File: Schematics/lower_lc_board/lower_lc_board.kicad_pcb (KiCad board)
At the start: 4 copper layers, 69.5 x 60 mm, 178 parts, among them J1 Stack Male Edge Connector, J10 SOL_CONN, J11 Screw_Terminal_01x02, J2 SWD_CONN, J3 USB_C_CONN, J4 HALL-1, J5 HALL-2, J6 PT1, J7 Screw_Terminal_01x02, J8 PT1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

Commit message: start lower refactor
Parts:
- removed J1: Stack Male Edge Connector, Connector_PCBEdge:BUS_PCIexpress_x1
- added REF**: TerminalBlock_TE_282834-2_1x02_P2.54mm_Horizontal, TerminalBlock_TE-Connectivity:TerminalBlock_TE_282834-2_1x02_P2.54mm_Horizontal, F.Cu at (129.5, 102.1)
- added REF**: TerminalBlock_TE_282834-2_1x02_P2.54mm_Horizontal, TerminalBlock_TE-Connectivity:TerminalBlock_TE_282834-2_1x02_P2.54mm_Horizontal, F.Cu at (136.9, 102.1)
- moved BZ1 30.0 mm to (202.0, 46.7)
- moved D8 30.0 mm to (202.2, 49.6)
- moved Q4 30.0 mm to (198.4, 48.8)
- moved R47 30.0 mm to (202.0, 51.4)
- moved C24 30.0 mm to (198.9, 51.4)
- moved R21 30.0 mm to (195.0, 46.7)
- moved R46 30.0 mm to (195.0, 48.3)
- moved C8 23.9 mm to (140.5, 117.8)
- moved R17 22.0 mm to (120.9, 114.0)
- moved C23 22.0 mm to (117.6, 116.0)
- moved J5 22.0 mm to (124.1, 114.0)
- moved R18 22.0 mm to (122.4, 113.9)
- moved C33 22.0 mm to (129.9, 116.9)
- moved J4 22.0 mm to (113.2, 114.0)
- moved C35 14.1 mm to (135.1, 117.1)
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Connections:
- J4 pad 1: GND -> +3V3
- J4 pad 4: +3V3 -> GND
- J5 pad 1: GND -> +3V3
- J5 pad 4: +3V3 -> GND
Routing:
- net +3V3: track 435.2 -> 356.2 mm, vias 20 -> 16
- net GND: track 236.0 -> 194.1 mm, vias 204 -> 194
- net HALL_SDA: track 57.6 -> 33.5 mm, vias 2 -> 1
- net /Sensing Circuitry/VPT: track 41.2 -> 19.7 mm
- net BUZZ_IN: track 18.0 -> 0.00 mm
- net Net-(BZ1--): track 16.5 -> 0.00 mm, vias 2 -> 0
- net +24V: track 133.7 -> 117.3 mm, vias 5 -> 3
- net HALL_SCL: track 50.1 -> 38.3 mm, vias 2 -> 1
- net VPT-SW: track 36.4 -> 24.9 mm, vias 2 -> 1
- net Net-(U11-G): track 7.76 -> 0.00 mm
- net +5V: track 67.7 -> 61.3 mm
- net +24V_BP: track 41.9 -> 36.0 mm
- net /Power Circuitry/3V3_BP: track 19.9 -> 14.8 mm
- net Net-(Q4-G): track 4.18 -> 0.00 mm
- net Net-(Q3-G): track 3.78 -> 0.00 mm
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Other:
- outline, holes or cut-outs redrawn

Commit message: start lower refactor
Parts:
- removed C12: 10uF, Capacitor_SMD:CP_Elec_4x5.4
- removed J11, J7: Screw_Terminal_01x02, TerminalBlock_TE-Connectivity:TerminalBlock_TE_282834-2_1x02_P2.54mm_Horizontal
- removed J6, J8: PT1, ul_B02B-PASK-1:CONN_B02B-PASK-1_JST
- removed the REF** at (129.5, 102.1)
- removed the REF** at (136.9, 102.1)
- added C1: 10uF, Capacitor_SMD:CP_Elec_4x5.4, F.Cu at (157.1, 62.5)
- added J1: Conn_01x06, CONN_SD-4:CONN_SD-43045-001_06_MOL, F.Cu at (163.7, 56.9)
- added REF**: MOLEX_1053091102, NANO-V-CONN:MOLEX_1053091102, F.Cu at (158.7, 124.2)
- added REF**: MOLEX_1053091102, NANO-V-CONN:MOLEX_1053091102, F.Cu at (153.9, 138.2)
- added REF**: CONN_SD-105309-100_04_MOL, NANO-V-4-CONN:CONN_SD-105309-100_04_MOL, F.Cu at (123.1, 102.8)
- added REF**: CONN_SD-105309-100_04_MOL, NANO-V-4-CONN:CONN_SD-105309-100_04_MOL, F.Cu at (130.2, 102.8)
- added REF**: MOLEX_1053091102, NANO-V-CONN:MOLEX_1053091102, F.Cu at (153.9, 146.0)
- added REF**: MOLEX_1053091102, NANO-V-CONN:MOLEX_1053091102, F.Cu at (165.8, 122.3)
- moved TH1 64.3 mm to (85.1, 81.0)
- moved U2 60.7 mm to (217.0, 91.6)
- moved C32 60.5 mm to (82.8, 91.8)
- moved C31 60.5 mm to (85.9, 91.8)
- moved R26 60.5 mm to (87.4, 91.8)
- moved R57 60.5 mm to (92.0, 91.8)
- moved C54 60.5 mm to (93.5, 91.8)
- moved C55 60.5 mm to (90.5, 91.8)
- moved R24 60.5 mm to (84.4, 91.8)
- moved R28 60.5 mm to (81.3, 91.8)
- moved R59 60.5 mm to (89.0, 91.8)
- moved R1 42.9 mm to (198.1, 68.2)
- moved D1 39.7 mm to (195.6, 76.2)
- moved C7 30.9 mm to (198.3, 58.8)
- moved TP1 26.6 mm to (194.4, 69.2)
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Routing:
- net +3V3: track 356.2 -> 202.8 mm, vias 16 -> 10
- net GND: track 194.1 -> 134.7 mm, vias 194 -> 156
- net +5V: track 61.3 -> 20.6 mm, vias 5 -> 1
- net Net-(D9B-K1A2): track 49.3 -> 25.0 mm, vias 3 -> 2
- net Net-(D9A-K3A4): track 53.7 -> 30.4 mm, vias 6 -> 5
- net CAN_P: track 20.6 -> 41.8 mm, vias 0 -> 1
- net CAN_N: track 21.3 -> 41.7 mm, vias 0 -> 1
- net Net-(D18B-K1A2): track 40.0 -> 21.1 mm, vias 3 -> 2
- net /Sensing Circuitry/VPT: track 19.7 -> 1.06 mm
- net +24V_BP: track 36.0 -> 20.1 mm
- net Net-(D18A-K3A4): track 37.1 -> 22.9 mm, vias 3 -> 2
- net HALL_SCL: track 38.3 -> 25.6 mm
- net /Sensing Circuitry/TC_P_1: track 11.7 -> 0.00 mm
- net /Sensing Circuitry/TC_N_2: track 10.9 -> 0.09 mm
- net HALL_SDA: track 33.5 -> 25.2 mm
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- removed copper zone on F.Cu, net /Power Circuitry/3V3_USB
- removed copper zone on B.Cu, net GND
- removed copper zone on In1.Cu, net GND
- removed copper zone on In2.Cu, net GND
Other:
- board text added: "2.6mm height between board and nano connector thing"
- board text removed: "+ SD SC -"
- board text removed: "3V3"
- board text removed: "HALL-1"
- board text removed: "HALL-2"
- board text removed: "LDO"
- board text removed: "PMUX"
- board text removed: "VBP"
- board text removed: "VFLTR"
- board text removed: "VOUT"
- board text removed: "VSWD"
- board text removed: "VUSB"

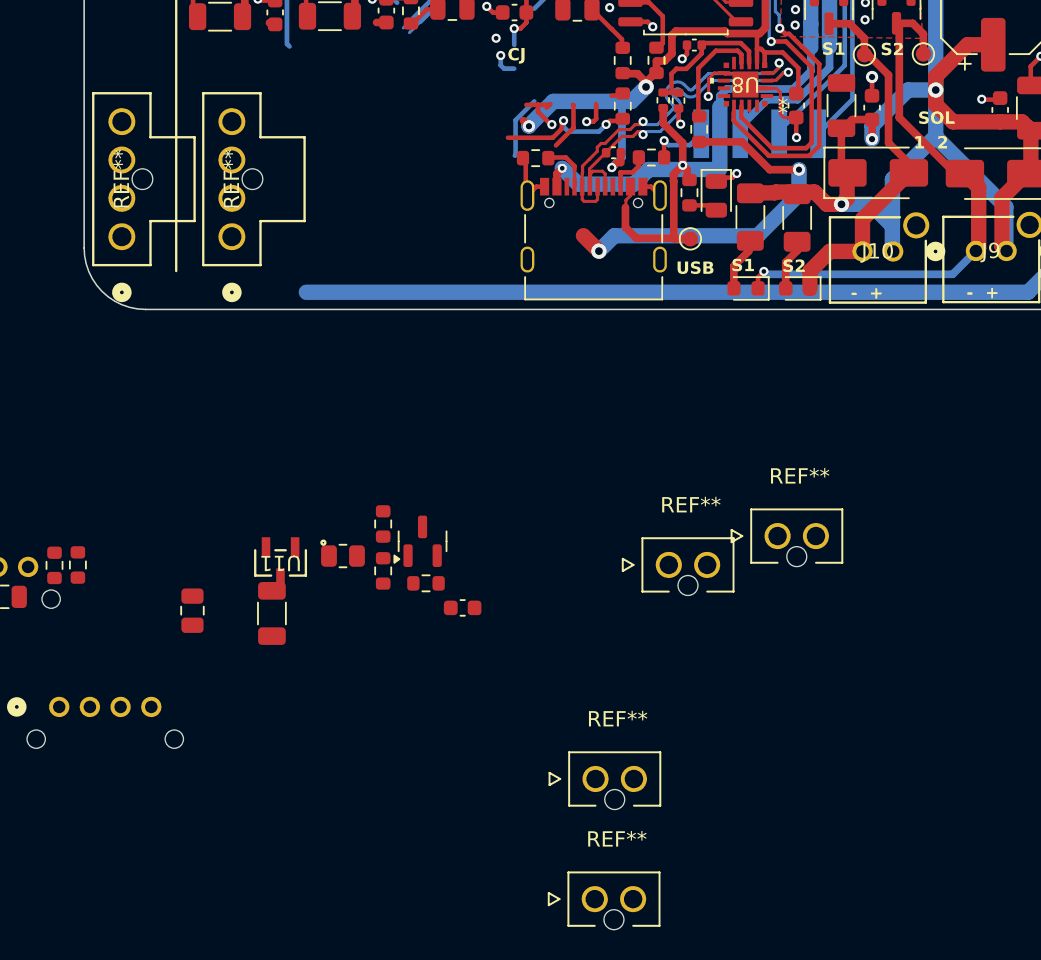
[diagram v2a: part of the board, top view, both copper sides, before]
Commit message: organize working copy of lower valve board for merge to main
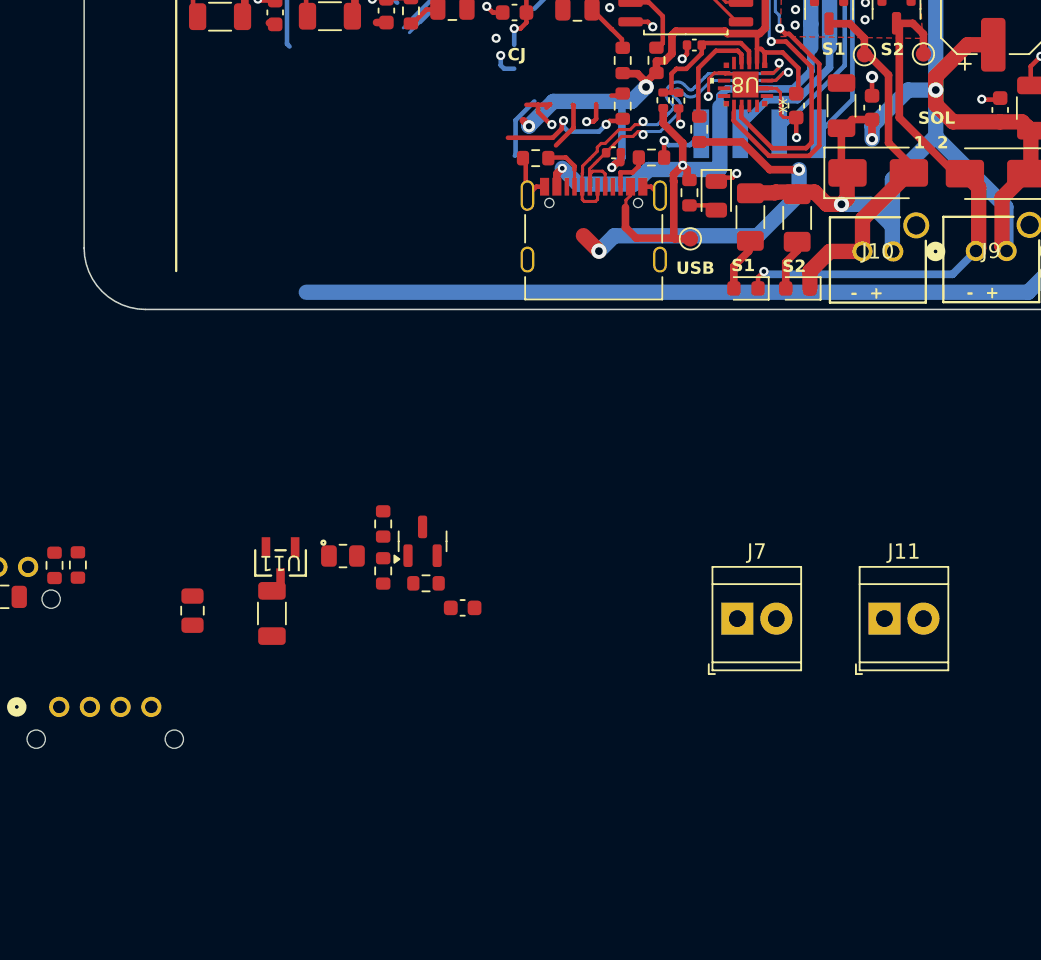
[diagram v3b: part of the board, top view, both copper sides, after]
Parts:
- removed REF** (x4): MOLEX_1053091102, NANO-V-CONN:MOLEX_1053091102
- removed REF** (x2): CONN_SD-105309-100_04_MOL, NANO-V-4-CONN:CONN_SD-105309-100_04_MOL
- added J11: Screw_Terminal_01x02, TerminalBlock_TE-Connectivity:TerminalBlock_TE_282834-2_1x02_P2.54mm_Horizontal, F.Cu at (172.8, 127.7)
- added J7: Screw_Terminal_01x02, TerminalBlock_TE-Connectivity:TerminalBlock_TE_282834-2_1x02_P2.54mm_Horizontal, F.Cu at (163.2, 127.7)

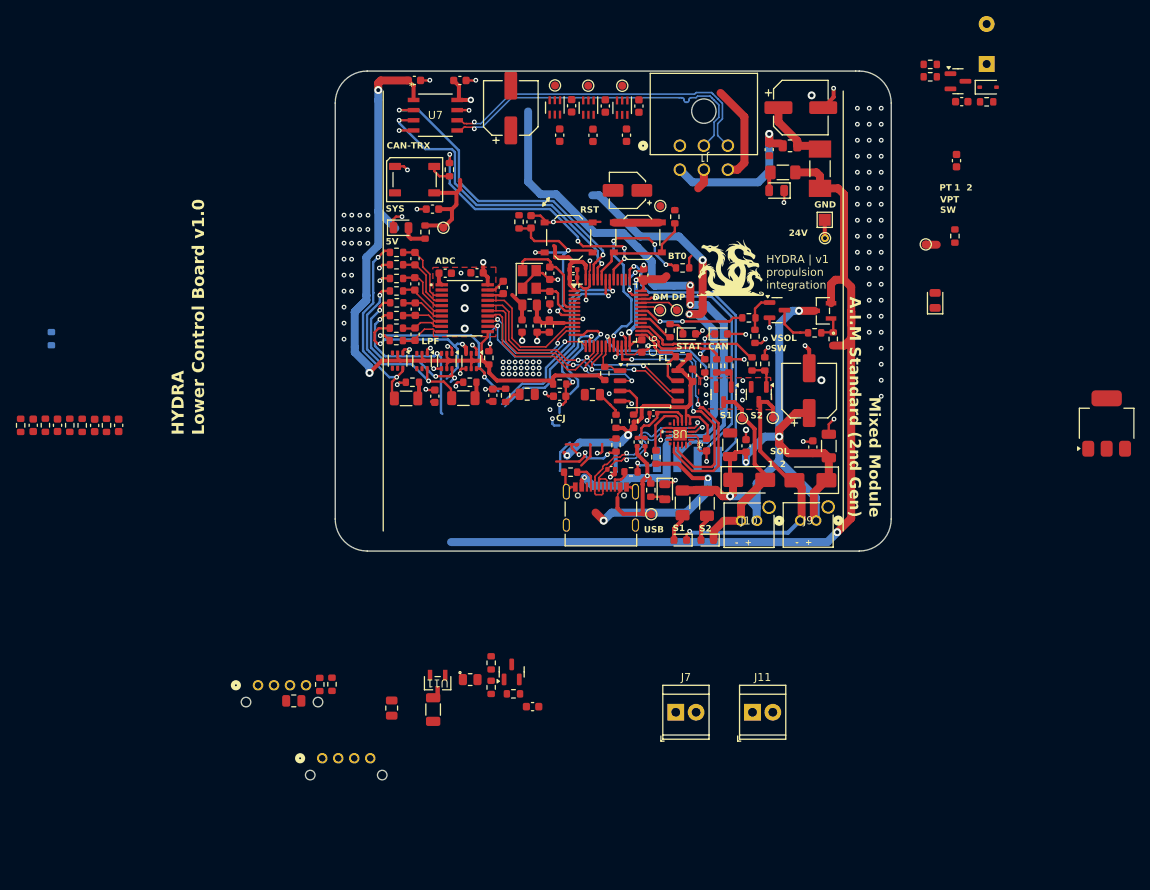
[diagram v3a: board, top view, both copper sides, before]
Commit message: lower refactor for review
 - curr using horziontal screw for TC
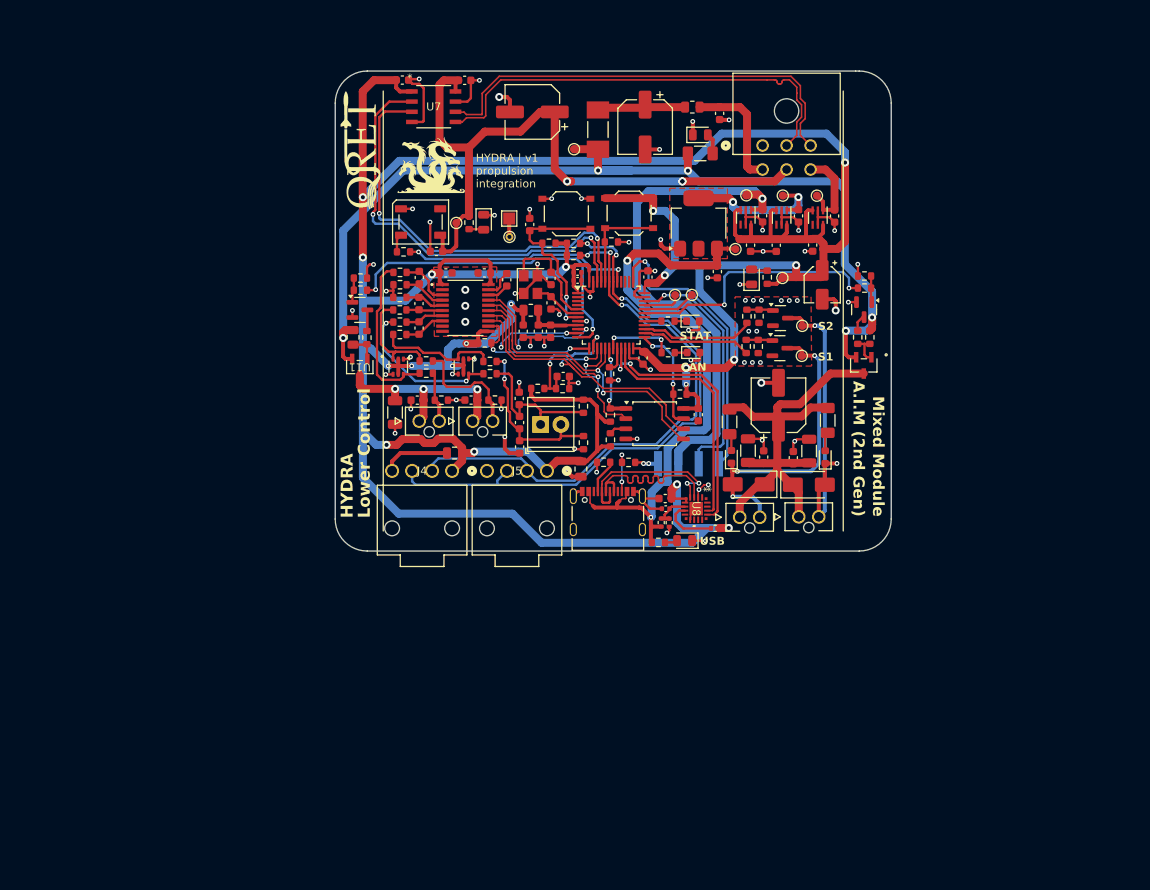
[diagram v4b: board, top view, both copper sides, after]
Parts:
- removed BZ1: Buzzer, Buzzer_Beeper:Buzzer_TDK_PS1240P02BT_D12.2mm_H6.5mm
- removed C24: 0.1uF, Capacitor_SMD:C_0603_1608Metric
- removed C25: 10nF, Capacitor_SMD:C_0603_1608Metric
- removed C53: 0.1uF, Capacitor_SMD:C_0805_2012Metric
- removed C54, C55: 1nF, Capacitor_SMD:C_0603_1608Metric
- removed the C8 at (145.3, 127.0)
- removed D14, D9: BAV199DW, Package_TO_SOT_SMD:SOT-363_SC-70-6
- removed D8: 1N4148WS-7-F, Diode_SMD:D_SOD-323
- removed J11: Screw_Terminal_01x02, TerminalBlock_TE-Connectivity:TerminalBlock_TE_282834-2_1x02_P2.54mm_Horizontal
- removed Q4: 2N7002, Package_TO_SOT_SMD:SOT-23
- removed R21: 10k, Resistor_SMD:R_0603_1608Metric
- removed R45: 1.5k, Capacitor_SMD:C_0402_1005Metric
- removed R46: 220, Resistor_SMD:R_0603_1608Metric
- removed R47, R55, R57: 1k, Resistor_SMD:R_0603_1608Metric
- removed R54, R59: 1M, Resistor_SMD:R_0603_1608Metric
- removed R56, R58: 200, Resistor_SMD:R_0603_1608Metric
- added J6: PT1, NANO-V-2-CONN:MOLEX_1053091102, F.Cu at (131.1, 91.3)
- added J8: PT1, NANO-V-2-CONN:MOLEX_1053091102, F.Cu at (137.8, 91.3)
- C30: footprint Capacitor_SMD:C_0805_2012Metric -> Capacitor_SMD:C_0603_1608Metric
- J10, J9: footprint ul_B02B-PASK-1:CONN_B02B-PASK-1_JST -> NANO-V-2-CONN:MOLEX_1053091102
- J4, J5: footprint S04B_PASK_2-P:CONN4_S04B-PASK_JST -> NANO-H-4-CONN:CONN_SD-105313-100_04_MOL; moved to F.Cu
- R13: footprint Resistor_SMD:R_0603_1608Metric -> Resistor_SMD:R_0402_1005Metric
- R32, R35: value 60 -> 62
- R33, R37: footprint Resistor_SMD:R_1206_3216Metric -> Resistor_SMD:R_0603_1608Metric
- TH1: moved to F.Cu
- moved R26 64.2 mm to (151.6, 89.5), turned to -90 degrees
- moved TH1 64.2 mm to (149.0, 87.2), turned to 0 degrees
- moved R18 62.8 mm to (150.4, 69.1), turned to 0 degrees
- moved R17 62.3 mm to (150.4, 70.6), turned to 180 degrees
- moved C32 60.9 mm to (143.7, 94.5)
- moved R28 59.2 mm to (139.9, 83.9), turned to 0 degrees
- moved C31 57.8 mm to (143.6, 88.5), turned to -90 degrees
- moved U2 56.8 mm to (166.0, 66.6)
- moved R24 56.0 mm to (139.9, 85.4), turned to 0 degrees
- moved R44 54.0 mm to (123.8, 74.9)
- moved R43 53.7 mm to (123.8, 73.4), turned to 180 degrees
- moved Q3 49.1 mm to (123.7, 77.4), turned to 0 degrees
- moved J5 45.6 mm to (147.1, 97.5)
- moved TP1 45.5 mm to (150.5, 57.3)
- moved R23 45.2 mm to (122.8, 80.8), turned to 90 degrees
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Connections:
- D13 pad 3: (no net) -> Net-(D13B-K1A2)
- D13 pad 4: (no net) -> GND
- D13 pad 5: (no net) -> +3V3
- D7 pad 2: Net-(D7-DOUT) -> unconnected-(D7-DOUT-Pad2)
- D7 pad 4: unconnected-(D7-DIN-Pad4) -> Net-(D7-DIN)
- J4 pad 2: HALL_SCL -> HALL_SDA
- J4 pad 3: HALL_SDA -> HALL_SCL
- J5 pad 2: HALL_SCL -> HALL_SDA
- J5 pad 3: HALL_SDA -> HALL_SCL
- R16 pad 1: Net-(D7-DOUT) -> Net-(D7-DIN)
- R37 pad 2: Net-(D14A-K3A4) -> Net-(D13B-K1A2)
- R38 pad 2: Net-(D14A-K3A4) -> Net-(D13B-K1A2)
- U9 pad 10: /Sensing Circuitry/TC_P_CLAMPED_1 -> GND
- U9 pad 7: /Sensing Circuitry/TC_P_CLAMPED_2 -> /Sensing Circuitry/TC_P_CLAMPED_1
- U9 pad 8: /Sensing Circuitry/TC_N_CLAMPED_2 -> /Sensing Circuitry/TC_N_CLAMPED_1
- U9 pad 9: /Sensing Circuitry/TC_N_CLAMPED_1 -> GND
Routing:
- net +3V3: track 202.8 -> 468.7 mm, vias 10 -> 20
- net +5V: track 20.6 -> 83.1 mm, vias 1 -> 3
- net HALL_SCL: track 25.6 -> 75.9 mm, vias 1 -> 3
- net HALL_SDA: track 25.2 -> 70.2 mm, vias 1 -> 3
- net GND: track 134.7 -> 173.6 mm, vias 156 -> 77
- net /Valve Control Circuitry/VSOL: track 87.8 -> 56.5 mm, vias 4 -> 0
- net Net-(D9A-K3A4): track 30.4 -> 0.00 mm, vias 5 -> 0
- net /Sensing Circuitry/VPT: track 1.06 -> 26.1 mm, vias 0 -> 3
- net Net-(D9B-K1A2): track 25.0 -> 0.00 mm, vias 2 -> 0
- net Net-(D14A-K3A4): track 24.4 -> 0.00 mm, vias 2 -> 0
- net BOOT1: track 26.0 -> 3.23 mm, vias 4 -> 0
- net VPT-SW: track 18.8 -> 41.2 mm, vias 1 -> 2
- net /Power Circuitry/3V3_USB: track 0.00 -> 19.7 mm, vias 0 -> 2
- net /Sensing Circuitry/TC_P_1: track 0.00 -> 19.0 mm
- net VSOL-SW: track 13.6 -> 32.5 mm
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- added copper zone on F.Cu, net /Power Circuitry/3V3_USB
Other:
- board text added: "A.I.M (2nd Gen)"
- board text added: "Hydra V1.0 QRET March 2026 Jeevan Sanchez"
- board text added: "Lower Control"
- board text removed: "- +"
- board text removed: "1 2"
- board text removed: "2.6mm height between board and nano connector thing"
- board text removed: "24V"
- board text removed: "5V"
- board text removed: "A.I.M Standard (2nd Gen)"
- board text removed: "ADC"
- board text removed: "BT0"
- board text removed: "CAN-TRX"
- board text removed: "CJ"
- board text removed: "DM DP"
- board text removed: "FL"
- board text removed: "GND"
- board text removed: "Hydra V1.0 QRET Feb 2026 Jeevan Sanchez"
- board text removed: "LPF"
- board text removed: "Lower Control Board v1.0"
- board text removed: "PT"
- board text removed: "RST"
- board text removed: "SOL"
- board text removed: "SYS"
- board text removed: "TC-1"
- board text removed: "TC-2"
- board text removed: "VPT SW"
- board text removed: "VSOL SW"
- board text removed: "bzz"
